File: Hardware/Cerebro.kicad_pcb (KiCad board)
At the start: 2 copper layers, 75 x 61.7 mm, 2 parts, among them U6 ATSAMD21G18A-AUT

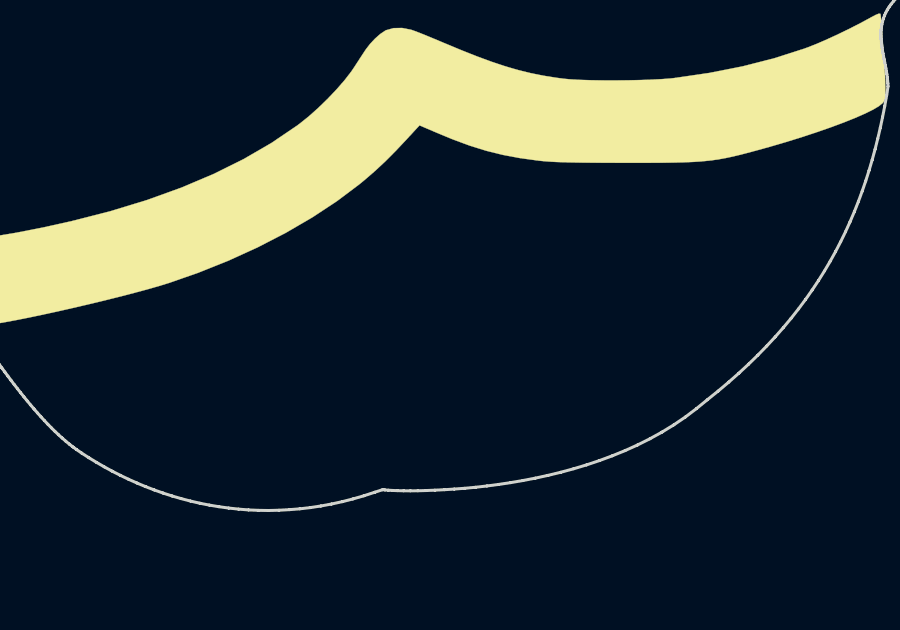
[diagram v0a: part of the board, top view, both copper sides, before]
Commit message: add logo
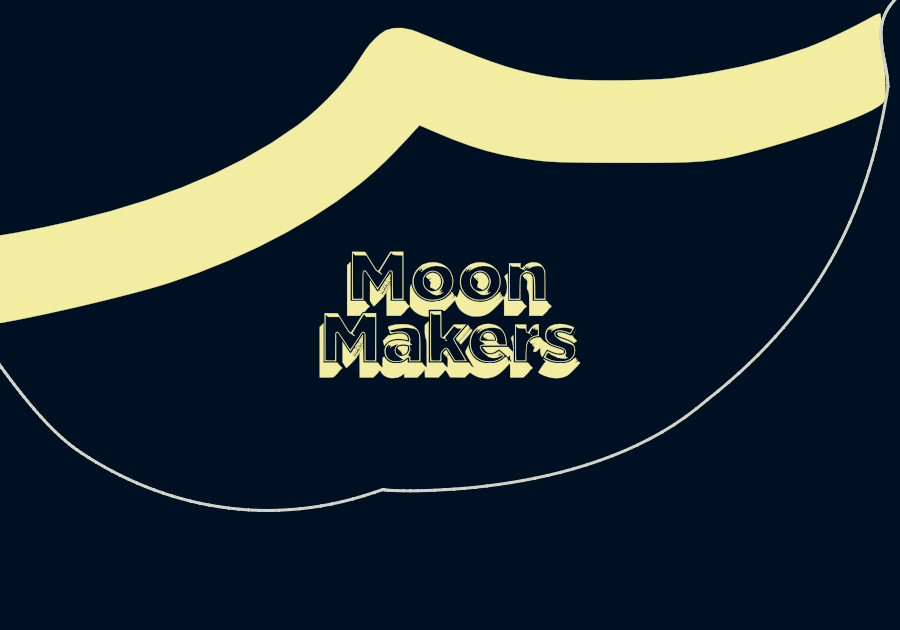
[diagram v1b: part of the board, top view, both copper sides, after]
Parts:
- added G***: LOGO, Aesthetics:MoonMakers_2, F.Cu at (161.8, 114.5)
- added G***: LOGO, Aesthetics:MoonMakers, B.Cu at (142.4, 71.7)

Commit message: update pcb
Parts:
- added svg2mod: G***, Aesthetics:heart, B.Cu at (142.7, 79.4)
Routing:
- net (no net): vias 0 -> 2
- added copper zone on B.Cu, net (none)
- added copper zone on F.Cu, net (none)
- removed copper zone on B.Cu, net GND
- removed copper zone on F.Cu, net GND
